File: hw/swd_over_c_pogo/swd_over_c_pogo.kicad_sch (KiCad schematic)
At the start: 4 parts, among them J1 AVR-ISP-6, P1 USB_C_Plug

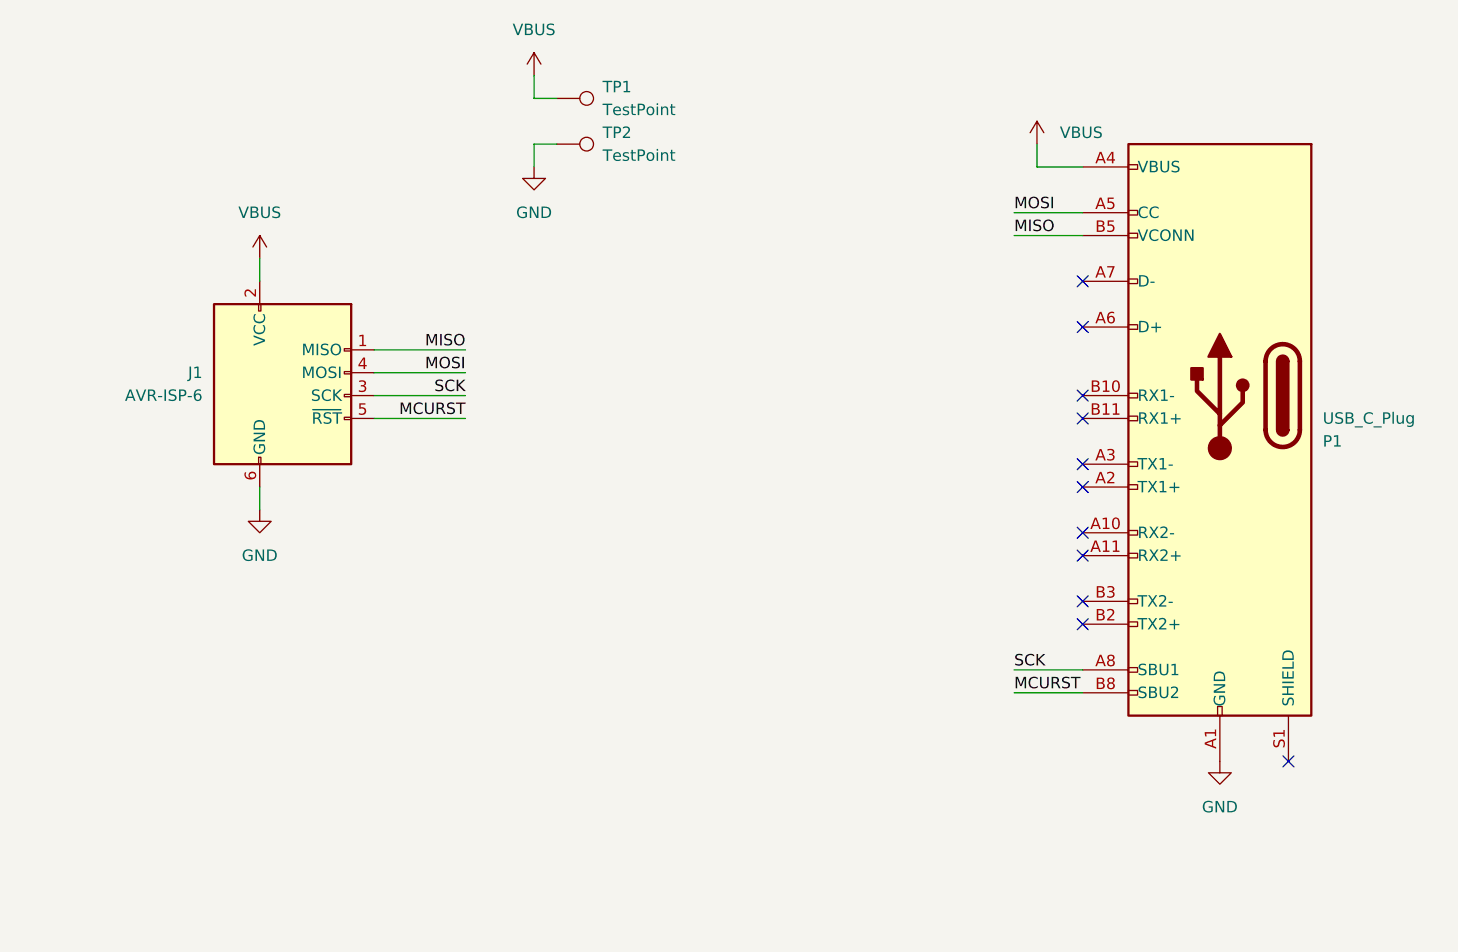
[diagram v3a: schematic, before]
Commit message: Make USB over C programmer v2.0 for JLC
Hopefully it works
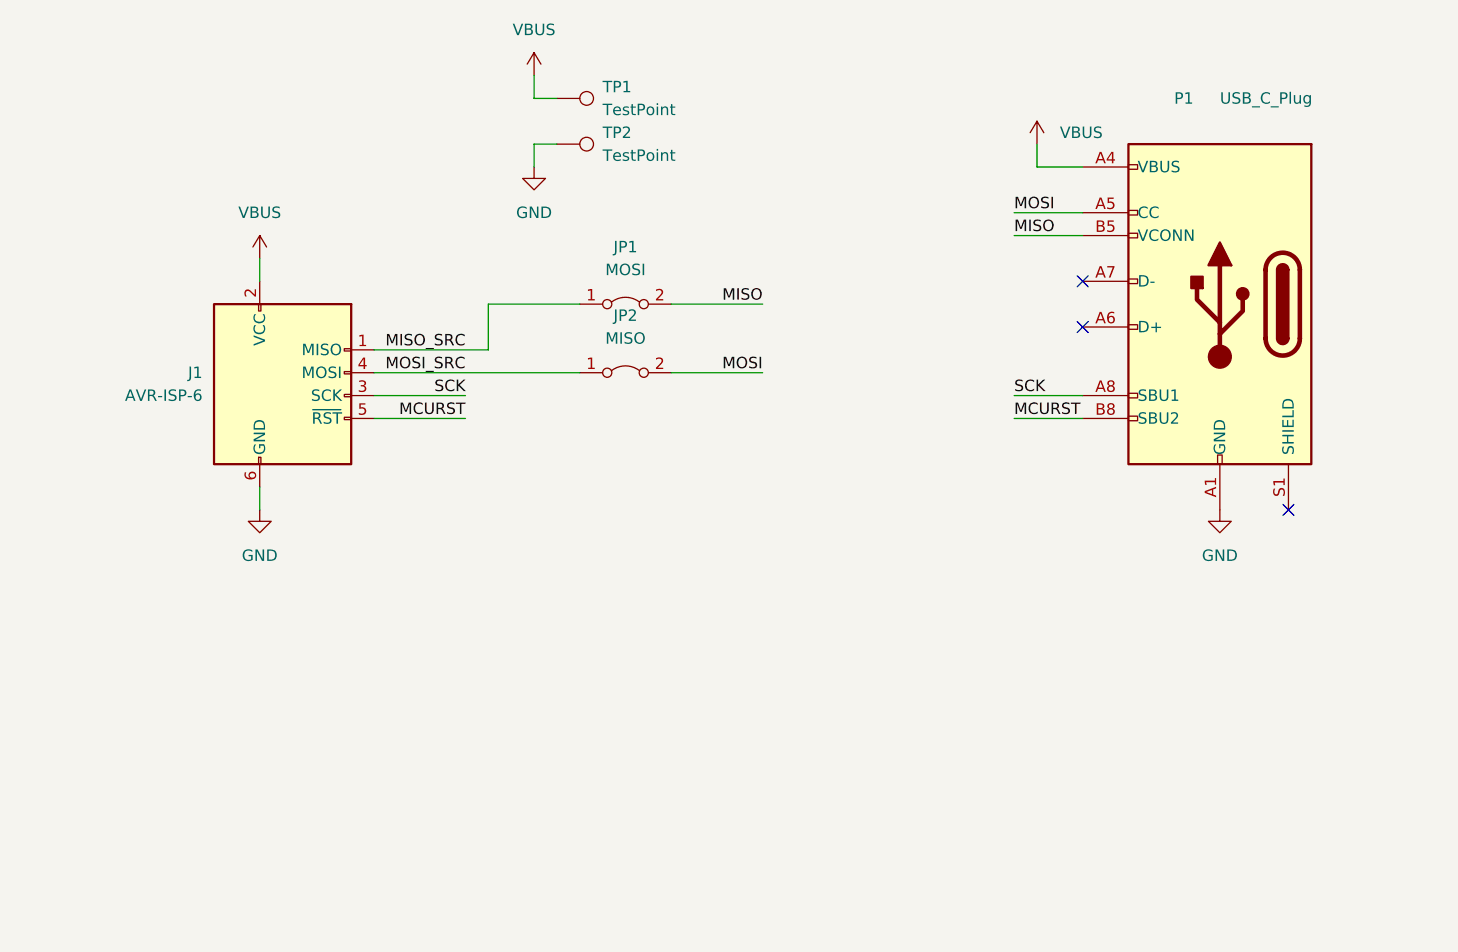
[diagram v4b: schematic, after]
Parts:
- added JP1: MOSI, Jumper:SolderJumper-2_P1.3mm_Bridged_RoundedPad1.0x1.5mm, symbol Jumper:Jumper_2_Bridged
- added JP2: MISO, Jumper:SolderJumper-2_P1.3mm_Bridged_RoundedPad1.0x1.5mm, symbol Jumper:Jumper_2_Bridged
- P1: footprint alvarop:USB4151-GF-C -> alvarop:TYPE-C-31-G-06; MPN USB4151-GF-C -> TYPE-C-31-G-06
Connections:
- net MISO: now also JP1.2 (B); no longer J1.1 (MISO)
- net MOSI: now also JP2.2 (B); no longer J1.4 (MOSI)
- new net MISO_SRC: J1.1 (MISO), JP1.1 (A)
- new net MOSI_SRC: J1.4 (MOSI), JP2.1 (A)
- no-connect marks 11 -> 3
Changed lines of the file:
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@@
   (title_block
     (title "Debugotron - SWD to USBC Programmer")
-    (date "2022-03-04")
-    (rev "1.2")
+    (date "2022-11-22")
+    (rev "2.0")
     (company "Quesadillon LLC")
   )
-  (no_connect (at 154.94 162.56))
-  (no_connect (at 132.08 147.32))
-  (no_connect (at 132.08 144.78))
-  (no_connect (at 132.08 121.92))
+  (no_connect (at 154.94 134.62))
   (no_connect (at 132.08 114.3))
   (no_connect (at 132.08 109.22))
-  (no_connect (at 132.08 139.7))
-  (no_connect (at 132.08 137.16))
-  (no_connect (at 132.08 132.08))
-  (no_connect (at 132.08 129.54))
-  (no_connect (at 132.08 124.46))
-  (wire (pts (xy 63.5 116.84) (xy 53.34 116.84))
+  (wire (pts (xy 53.34 116.84) (xy 66.04 116.84))
     (stroke (width 0) (type default) (color 0 0 0 0))
   )
@@
     (stroke (width 0) (type default) (color 0 0 0 0))
   )
-  (wire (pts (xy 132.08 154.94) (xy 124.46 154.94))
-    (stroke (width 0) (type default) (color 0 0 0 0))
-  )
-  (wire (pts (xy 63.5 119.38) (xy 53.34 119.38))
+  (wire (pts (xy 132.08 124.46) (xy 124.46 124.46))
+    (stroke (width 0) (type default) (color 0 0 0 0))
+  )
+  (wire (pts (xy 53.34 119.38) (xy 76.2 119.38))
+    (stroke (width 0) (type default) (color 0 0 0 0))
+  )
+  (wire (pts (xy 66.04 111.76) (xy 76.2 111.76))
+    (stroke (width 0) (type default) (color 0 0 0 0))
+  )
+  (wire (pts (xy 86.36 111.76) (xy 96.52 111.76))
     (stroke (width 0) (type default) (color 0 0 0 0))
   )
@@
     (stroke (width 0) (type default) (color 0 0 0 0))
   )
+  (wire (pts (xy 86.36 119.38) (xy 96.52 119.38))
+    (stroke (width 0) (type default) (color 0 0 0 0))
+  )
+  (wire (pts (xy 66.04 116.84) (xy 66.04 111.76))
+    (stroke (width 0) (type default) (color 0 0 0 0))
+  )
   (wire (pts (xy 40.64 132.08) (xy 40.64 134.62))
     (stroke (width 0) (type default) (color 0 0 0 0))
   )
-  (wire (pts (xy 132.08 152.4) (xy 124.46 152.4))
+  (wire (pts (xy 132.08 121.92) (xy 124.46 121.92))
     (stroke (width 0) (type default) (color 0 0 0 0))
   )
@@
     (effects (font (size 1.27 1.27)) (justify right bottom))
   )
-  (label "SCK" (at 124.46 152.4 0)
+  (label "SCK" (at 124.46 121.92 0)
     (effects (font (size 1.27 1.27)) (justify left bottom))
   )
-  (label "MCURST" (at 124.46 154.94 0)
+  (label "MCURST" (at 124.46 124.46 0)
     (effects (font (size 1.27 1.27)) (justify left bottom))
   )
-  (label "MISO" (at 63.5 116.84 180)
+  (label "MISO_SRC" (at 63.5 116.84 180)
     (effects (font (size 1.27 1.27)) (justify right bottom))
   )
@@
     (effects (font (size 1.27 1.27)) (justify left bottom))
   )
-  (label "MOSI" (at 63.5 119.38 180)
+  (label "MISO" (at 96.52 111.76 180)
+    (effects (font (size 1.27 1.27)) (justify right bottom))
+  )
+  (label "MOSI_SRC" (at 63.5 119.38 180)
     (effects (font (size 1.27 1.27)) (justify right bottom))
   )
@@
     (effects (font (size 1.27 1.27)) (justify left bottom))
   )
+  (label "MOSI" (at 96.52 119.38 180)
+    (effects (font (size 1.27 1.27)) (justify right bottom))
+  )
   (label "MCURST" (at 63.5 124.46 180)
     (effects (font (size 1.27 1.27)) (justify right bottom))
+  )
+  (symbol (lib_id "Jumper:Jumper_2_Bridged") (at 81.28 119.38 0) (unit 1)
+    (in_bom yes) (on_board yes) (fields_autoplaced)
+    (property "Reference" "JP2" (id 0) (at 81.28 113.03 0))
+    (property "Value" "MISO" (id 1) (at 81.28 115.57 0))
+    (property "Footprint" "Jumper:SolderJumper-2_P1.3mm_Bridged_RoundedPad1.0x1.5mm" (id 2) (at 81.28 119.38 0)
+      (effects (font (size 1.27 1.27)) hide)
+    )
+    (property "Datasheet" "~" (id 3) (at 81.28 119.38 0)
+      (effects (font (size 1.27 1.27)) hide)
+    )
+    (pin "1")
+    (pin "2")
   )
   (symbol (lib_id "power:GND") (at 40.64 134.62 0) (unit 1)
@@
   (symbol (lib_id "Connector:USB_C_Plug") (at 147.32 121.92 0) (mirror y) (unit 1)
     (in_bom yes) (on_board yes) (fields_autoplaced)
-    (property "Reference" "P1" (id 0) (at 158.75 127.0001 0)
-      (effects (font (size 1.27 1.27)) (justify right))
-    )
-    (property "Value" "USB_C_Plug" (id 1) (at 158.75 124.4601 0)
-      (effects (font (size 1.27 1.27)) (justify right))
-    )
-    (property "Footprint" "alvarop:USB4151-GF-C" (id 2) (at 143.51 121.92 0)
-      (effects (font (size 1.27 1.27)) hide)
-    )
-    (property "Datasheet" "https://www.usb.org/sites/default/files/documents/usb_type-c.zip" (id 3) (at 143.51 121.92 0)
-      (effects (font (size 1.27 1.27)) hide)
-    )
-    (property "MPN" " USB4151-GF-C" (id 4) (at 147.32 121.92 0)
+    (property "Reference" "P1" (id 0) (at 142.24 88.9 0)
+      (effects (font (size 1.27 1.27)) (justify right))
+    )
+    (property "Value" "USB_C_Plug" (id 1) (at 147.32 88.9 0)
+      (effects (font (size 1.27 1.27)) (justify right))
+    )
+    (property "Footprint" "alvarop:TYPE-C-31-G-06" (id 2) (at 132.08 137.16 0)
+      (effects (font (size 1.27 1.27)) hide)
+    )
+    (property "Datasheet" "" (id 3) (at 149.86 91.44 0)
+      (effects (font (size 1.27 1.27)) hide)
+    )
+    (property "MPN" "TYPE-C-31-G-06" (id 4) (at 134.62 134.62 0)
       (effects (font (size 1.27 1.27)) hide)
     )
     (pin "A1")
-    (pin "A10")
-    (pin "A11")
     (pin "A12")
-    (pin "A2")
-    (pin "A3")
     (pin "A4")
     (pin "A5")
@@
     (pin "A9")
     (pin "B1")
-    (pin "B10")
-    (pin "B11")
     (pin "B12")
-    (pin "B2")
-    (pin "B3")
     (pin "B4")
     (pin "B5")
@@
     (pin "1")
   )
-  (symbol (lib_id "power:GND") (at 147.32 162.56 0) (unit 1)
-    (in_bom yes) (on_board yes) (fields_autoplaced)
-    (property "Reference" "#PWR04" (id 0) (at 147.32 168.91 0)
-      (effects (font (size 1.27 1.27)) hide)
-    )
-    (property "Value" "GND" (id 1) (at 147.32 167.64 0))
-    (property "Footprint" "" (id 2) (at 147.32 162.56 0)
-      (effects (font (size 1.27 1.27)) hide)
-    )
-    (property "Datasheet" "" (id 3) (at 147.32 162.56 0)
+  (symbol (lib_id "Jumper:Jumper_2_Bridged") (at 81.28 111.76 0) (unit 1)
+    (in_bom yes) (on_board yes) (fields_autoplaced)
+    (property "Reference" "JP1" (id 0) (at 81.28 105.41 0))
+    (property "Value" "MOSI" (id 1) (at 81.28 107.95 0))
+    (property "Footprint" "Jumper:SolderJumper-2_P1.3mm_Bridged_RoundedPad1.0x1.5mm" (id 2) (at 81.28 111.76 0)
+      (effects (font (size 1.27 1.27)) hide)
+    )
+    (property "Datasheet" "~" (id 3) (at 81.28 111.76 0)
+      (effects (font (size 1.27 1.27)) hide)
+    )
+    (pin "1")
+    (pin "2")
+  )
+  (symbol (lib_id "power:GND") (at 147.32 134.62 0) (unit 1)
+    (in_bom yes) (on_board yes) (fields_autoplaced)
+    (property "Reference" "#PWR04" (id 0) (at 147.32 140.97 0)
+      (effects (font (size 1.27 1.27)) hide)
+    )
+    (property "Value" "GND" (id 1) (at 147.32 139.7 0))
+    (property "Footprint" "" (id 2) (at 147.32 134.62 0)
+      (effects (font (size 1.27 1.27)) hide)
+    )
+    (property "Datasheet" "" (id 3) (at 147.32 134.62 0)
       (effects (font (size 1.27 1.27)) hide)
     )
@@
       (reference "J1") (unit 1) (value "AVR-ISP-6") (footprint "Connector_IDC:IDC-Header_2x03_P2.54mm_Vertical")
     )
+    (path "/b702d347-b3da-45db-aeb2-114e93e3aec6"
+      (reference "JP1") (unit 1) (value "MOSI") (footprint "Jumper:SolderJumper-2_P1.3mm_Bridged_RoundedPad1.0x1.5mm")
+    )
+    (path "/02115a6a-4485-40e4-9e71-2bd79b477fc3"
+      (reference "JP2") (unit 1) (value "MISO") (footprint "Jumper:SolderJumper-2_P1.3mm_Bridged_RoundedPad1.0x1.5mm")
+    )
     (path "/3a507fa3-99cb-4860-90db-ecba158074f5"
-      (reference "P1") (unit 1) (value "USB_C_Plug") (footprint "alvarop:USB4151-GF-C")
+      (reference "P1") (unit 1) (value "USB_C_Plug") (footprint "alvarop:TYPE-C-31-G-06")
     )
     (path "/31d45c1b-7aed-47cb-958e-e0be400cc9c7"
